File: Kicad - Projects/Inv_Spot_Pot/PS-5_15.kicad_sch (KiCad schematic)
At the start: 23 parts, among them U2 LTV-817S

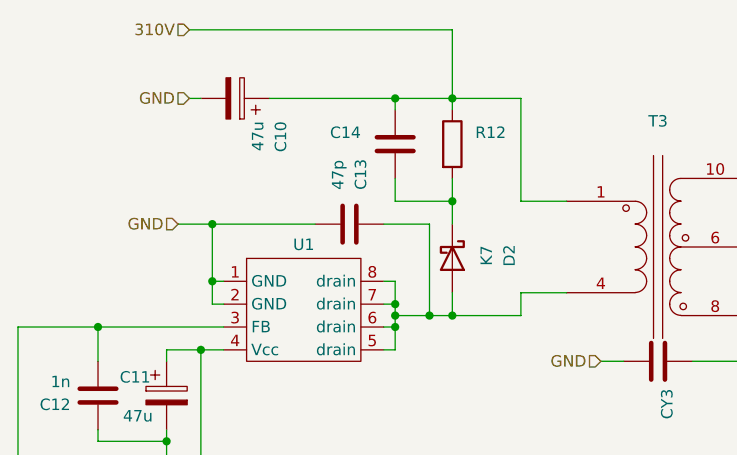
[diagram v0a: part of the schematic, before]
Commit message: Semi-final Touches
Menu now uses power instead of current

Removed pulsed timing from "CARVAO" and "ARRUELA" operation modes

Added parafix mode

Fixed schematic for output transformer

Added rectification on the output

Trying different power trace geometry in antecipation of voltage spikes
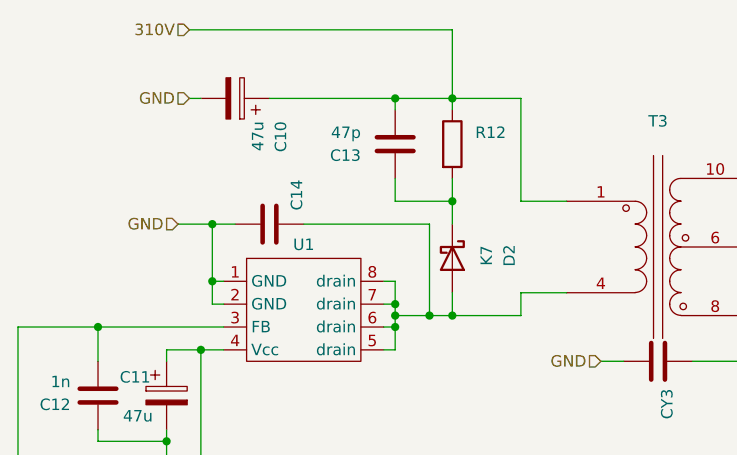
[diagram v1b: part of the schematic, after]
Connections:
- net 310V: now also C13.2; no longer C14.1
- net GND: now also C14.1; no longer C13.2
- net at D2.2 (A), T3.4, U1.5 (drain)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: now also C14.2; no longer C13.1
- net at D2.1 (K), R12.2: now also C13.1; no longer C14.2
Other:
- moved on the sheet: C13, C14
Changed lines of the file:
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@@
+	)
+	(junction
+		(at 104.14 71.12)
+		(diameter 0)
+		(color 0 0 0 0)
+	)
+	(junction
+		(at 83.82 85.09)
+		(diameter 0)
+		(color 0 0 0 0)
 	)
 	(junction
@@
 	)
 	(junction
-		(at 104.14 71.12)
-		(diameter 0)
-		(color 0 0 0 0)
-	)
-	(junction
 		(at 110.49 82.55)
 		(diameter 0)
@@
 	)
 	(junction
-		(at 83.82 85.09)
-		(diameter 0)
-		(color 0 0 0 0)
-	)
-	(junction
 		(at 83.82 91.44)
 		(diameter 0)
@@
 	(wire
 		(pts
-			(xy 102.87 85.09) (xy 107.95 85.09)
-		)
-		(stroke
-			(width 0)
-			(type default)
-		)
-	)
-	(wire
-		(pts
 			(xy 62.23 125.73) (xy 62.23 96.52)
 		)
@@
 	(wire
 		(pts
+			(xy 104.14 71.12) (xy 110.49 71.12)
+		)
+		(stroke
+			(width 0)
+			(type default)
+		)
+	)
+	(wire
+		(pts
 			(xy 76.2 113.03) (xy 78.74 113.03)
 		)
@@
 	(wire
 		(pts
+			(xy 104.14 71.12) (xy 104.14 72.39)
+		)
+		(stroke
+			(width 0)
+			(type default)
+		)
+	)
+	(wire
+		(pts
 			(xy 123.19 92.71) (xy 118.11 92.71)
 		)
@@
 	(wire
 		(pts
+			(xy 104.14 80.01) (xy 104.14 82.55)
+		)
+		(stroke
+			(width 0)
+			(type default)
+		)
+	)
+	(wire
+		(pts
 			(xy 83.82 91.44) (xy 85.09 91.44)
 		)
@@
 	(wire
 		(pts
-			(xy 104.14 80.01) (xy 104.14 82.55)
+			(xy 93.98 85.09) (xy 107.95 85.09)
 		)
 		(stroke
@@
 	(wire
 		(pts
-			(xy 83.82 85.09) (xy 95.25 85.09)
-		)
-		(stroke
-			(width 0)
-			(type default)
-		)
-	)
-	(wire
-		(pts
-			(xy 104.14 71.12) (xy 104.14 72.39)
-		)
-		(stroke
-			(width 0)
-			(type default)
-		)
-	)
-	(wire
-		(pts
 			(xy 143.51 95.25) (xy 144.78 95.25)
 		)
@@
 	(wire
 		(pts
-			(xy 110.49 71.12) (xy 104.14 71.12)
-		)
-		(stroke
-			(width 0)
-			(type default)
-		)
-	)
-	(wire
-		(pts
 			(xy 110.49 82.55) (xy 110.49 85.09)
 		)
@@
 		(pts
 			(xy 107.95 85.09) (xy 107.95 95.25)
+		)
+		(stroke
+			(width 0)
+			(type default)
+		)
+	)
+	(wire
+		(pts
+			(xy 83.82 85.09) (xy 86.36 85.09)
 		)
 		(stroke
@@
 		)
 	)
-	(netclass_flag ""
-		(length 2.54)
-		(shape round)
-		(at 110.49 82.55 270)
-		(fields_autoplaced yes)
-		(effects
-			(font
-				(size 1.27 1.27)
-			)
-			(justify right bottom)
-		)
-		(property "Classes da rede" "HVLC"
-			(at 113.03 81.8515 90)
-			(show_name no)
-			(do_not_autoplace no)
-			(effects
-				(font
-					(size 1.27 1.27)
-				)
-				(justify left)
-			)
-		)
-		(property "Component Class" ""
-			(at -36.83 13.97 0)
-			(show_name no)
-			(do_not_autoplace no)
-			(effects
-				(font
-					(size 1.27 1.27)
-					(italic yes)
-				)
-			)
-		)
-	)
 	(symbol
 		(lib_id "Device:C")
-		(at 99.06 85.09 270)
-		(mirror x)
+		(at 104.14 76.2 180)
 		(unit 1)
 		(body_style 1)
@@
 		(dnp no)
 		(property "Reference" "C13"
-			(at 100.3301 81.28 0)
+			(at 100.33 77.4701 0)
 			(show_name no)
 			(do_not_autoplace no)
@@
 		)
 		(property "Value" "47p"
-			(at 97.7901 81.28 0)
+			(at 100.33 74.9301 0)
 			(show_name no)
 			(do_not_autoplace no)
@@
 		)
 		(property "Footprint" "Capacitor_THT:C_Disc_D8.0mm_W5.0mm_P7.50mm"
-			(at 95.25 84.1248 0)
+			(at 103.1748 72.39 0)
 			(hide yes)
 			(show_name no)
@@
 		)
 		(property "Datasheet" ""
-			(at 99.06 85.09 0)
+			(at 104.14 76.2 0)
 			(hide yes)
 			(show_name no)
@@
 		)
 		(property "Description" "Unpolarized capacitor"
-			(at 99.06 85.09 0)
+			(at 104.14 76.2 0)
 			(hide yes)
 			(show_name no)
@@
 	(symbol
 		(lib_id "Device:C")
-		(at 104.14 76.2 0)
-		(mirror y)
+		(at 90.17 85.09 90)
 		(unit 1)
 		(body_style 1)
@@
 		(dnp no)
 		(property "Reference" "C14"
-			(at 100.33 74.9299 0)
+			(at 93.218 83.566 0)
 			(show_name no)
 			(do_not_autoplace no)
@@
 		)
 		(property "Value" "100n"
-			(at 100.33 77.4699 0)
+			(at 91.4399 81.28 0)
 			(hide yes)
 			(show_name no)
@@
 		)
 		(property "Footprint" "Capacitor_SMD:C_1206_3216Metric_Pad1.33x1.80mm_HandSolder"
-			(at 103.1748 80.01 0)
+			(at 93.98 84.1248 0)
 			(hide yes)
 			(show_name no)
@@
 		)
 		(property "Datasheet" ""
-			(at 104.14 76.2 0)
+			(at 90.17 85.09 0)
 			(hide yes)
 			(show_name no)
@@
 		)
 		(property "Description" "Unpolarized capacitor"
-			(at 104.14 76.2 0)
+			(at 90.17 85.09 0)
 			(hide yes)
 			(show_name no)
